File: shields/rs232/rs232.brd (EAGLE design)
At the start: 35.6 x 26.7 mm, 33 parts, among them Q5 2.5A/30V/105mΩ, Q6 2.5A/30V/105mΩ, Q7 2.5A/30V/105mΩ, Q8 2.5A/30V/105mΩ, U2 MAX3232, U3 OPENMV3

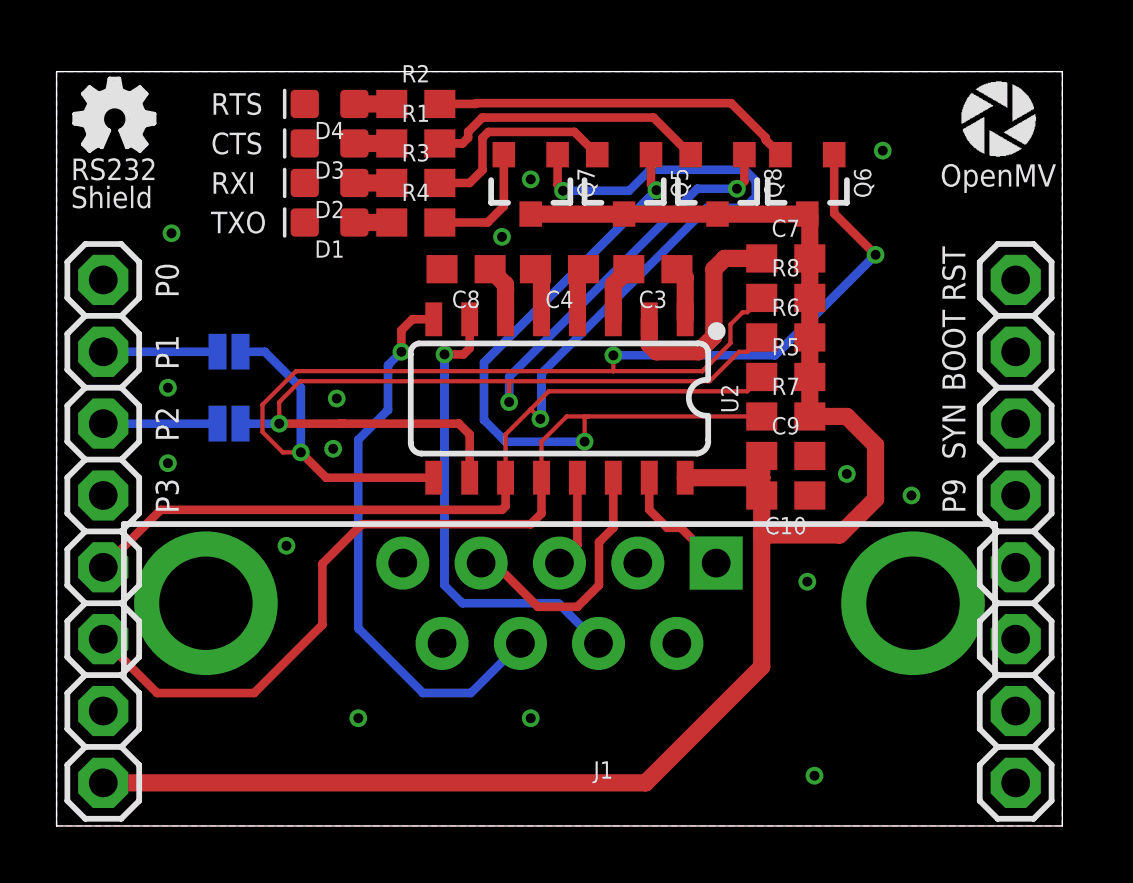
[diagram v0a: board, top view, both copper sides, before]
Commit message: Fix rs232 shield
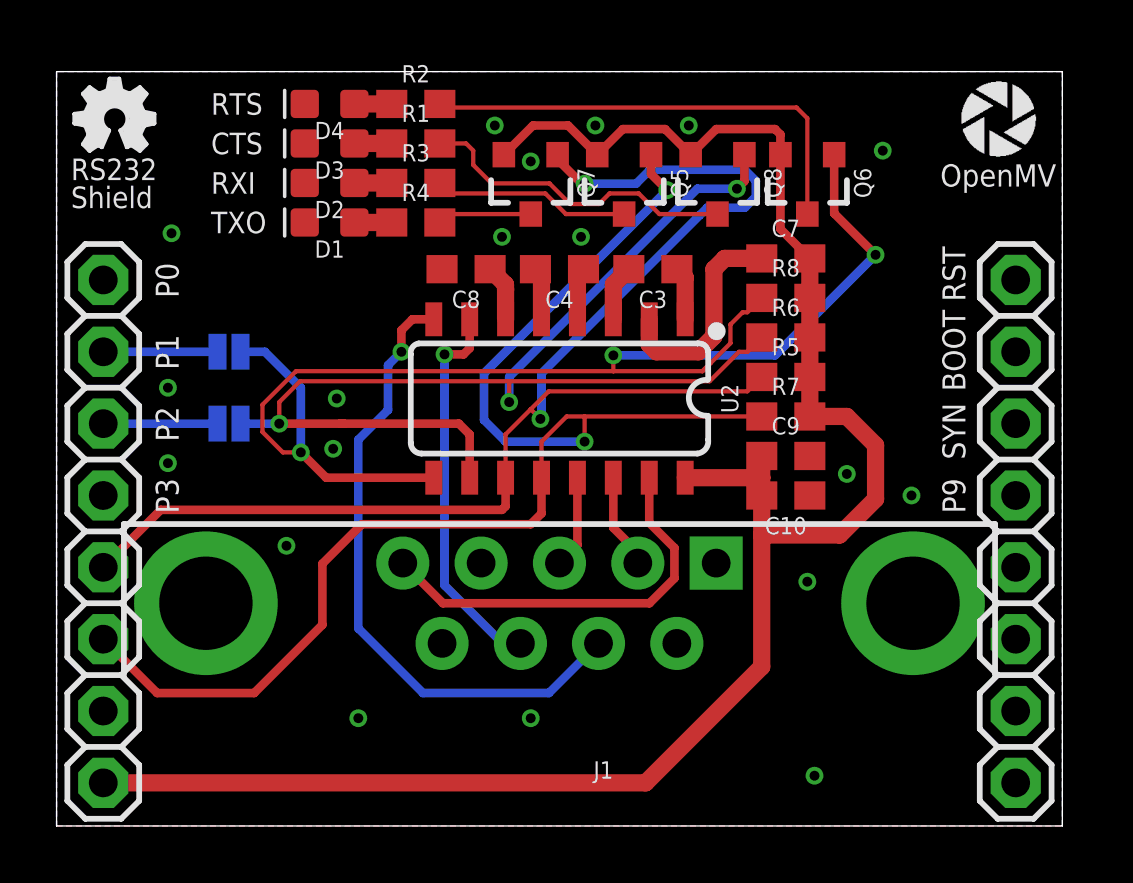
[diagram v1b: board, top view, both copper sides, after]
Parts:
- J1: device SparkFun-Connectors:DB9_MALE -> SparkFun-Connectors:DB9
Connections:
- net 3V3: now also Q5.2, Q6.2, Q7.2, Q8.2; no longer Q5.3, Q6.3, Q7.3, Q8.3
- net N$10: now also Q8.3; no longer Q8.2
- net N$6: now also Q7.3; no longer Q7.2
- net N$7: now also Q5.3; no longer Q5.2
- net N$8: now also Q6.3; no longer Q6.2
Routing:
- net GND: track 4.28 -> 14.5 mm, vias 15 -> 19
- net RS232_TXO: track 9.14 -> 3.38 mm
- net 3V3: track 61.7 -> 66.6 mm
- net N$8: track 12.9 -> 16.6 mm
- net RS232_RTS_I: track 19.9 -> 22.6 mm
- net RS232_CTS_O: track 16.5 -> 13.7 mm
- net N$10: track 9.92 -> 11.5 mm
- net N$6: track 4.32 -> 3.34 mm
- net TXO: track 49.1 -> 48.4 mm
